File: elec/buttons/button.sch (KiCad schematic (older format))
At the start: 6 parts, among them SW1 SW_PUSH, U1 moteino

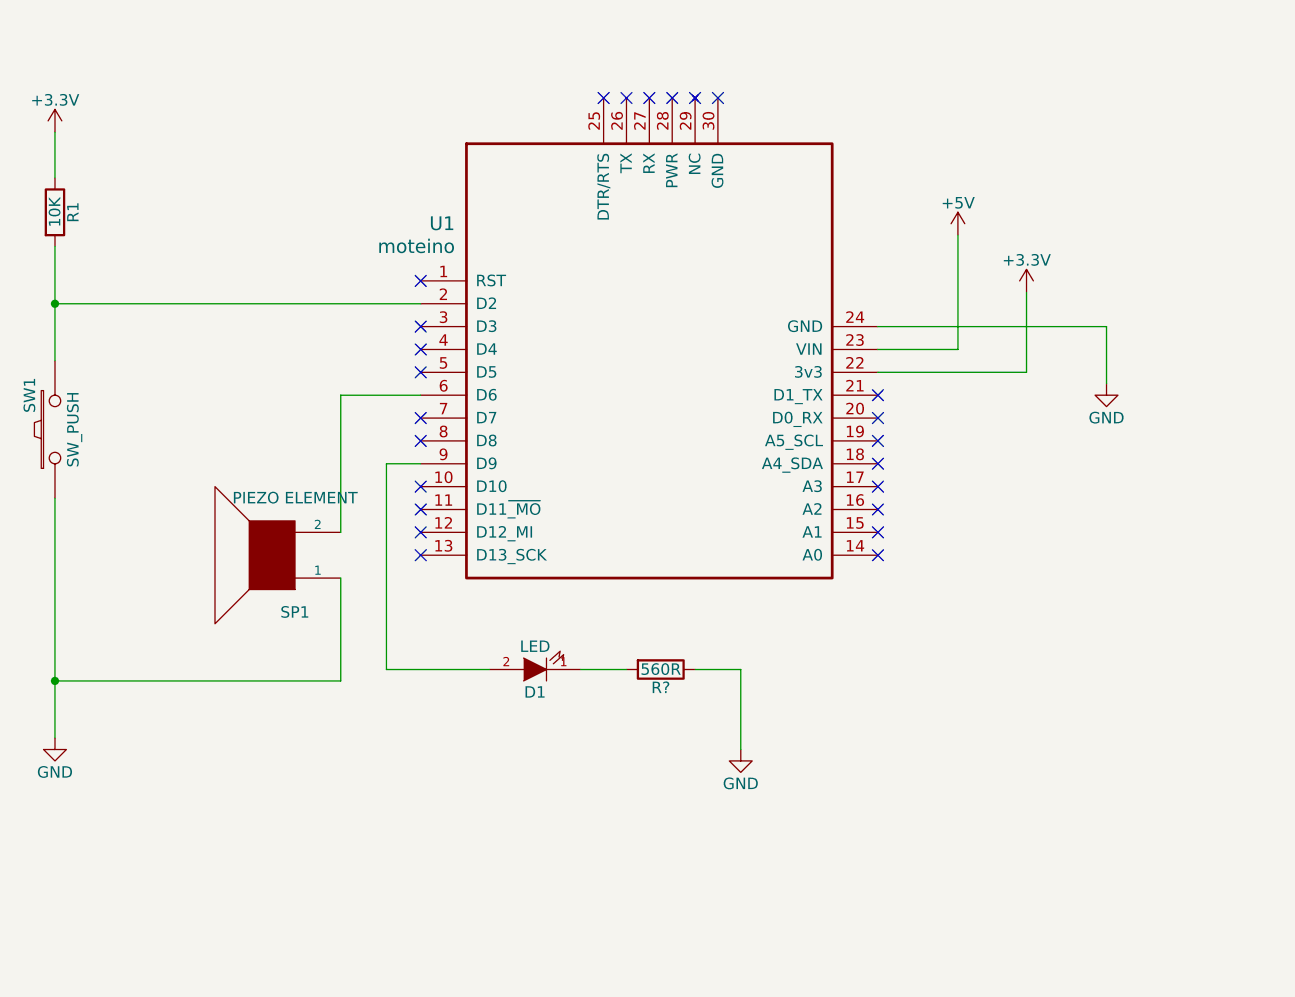
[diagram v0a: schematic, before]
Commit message: updated button schematic
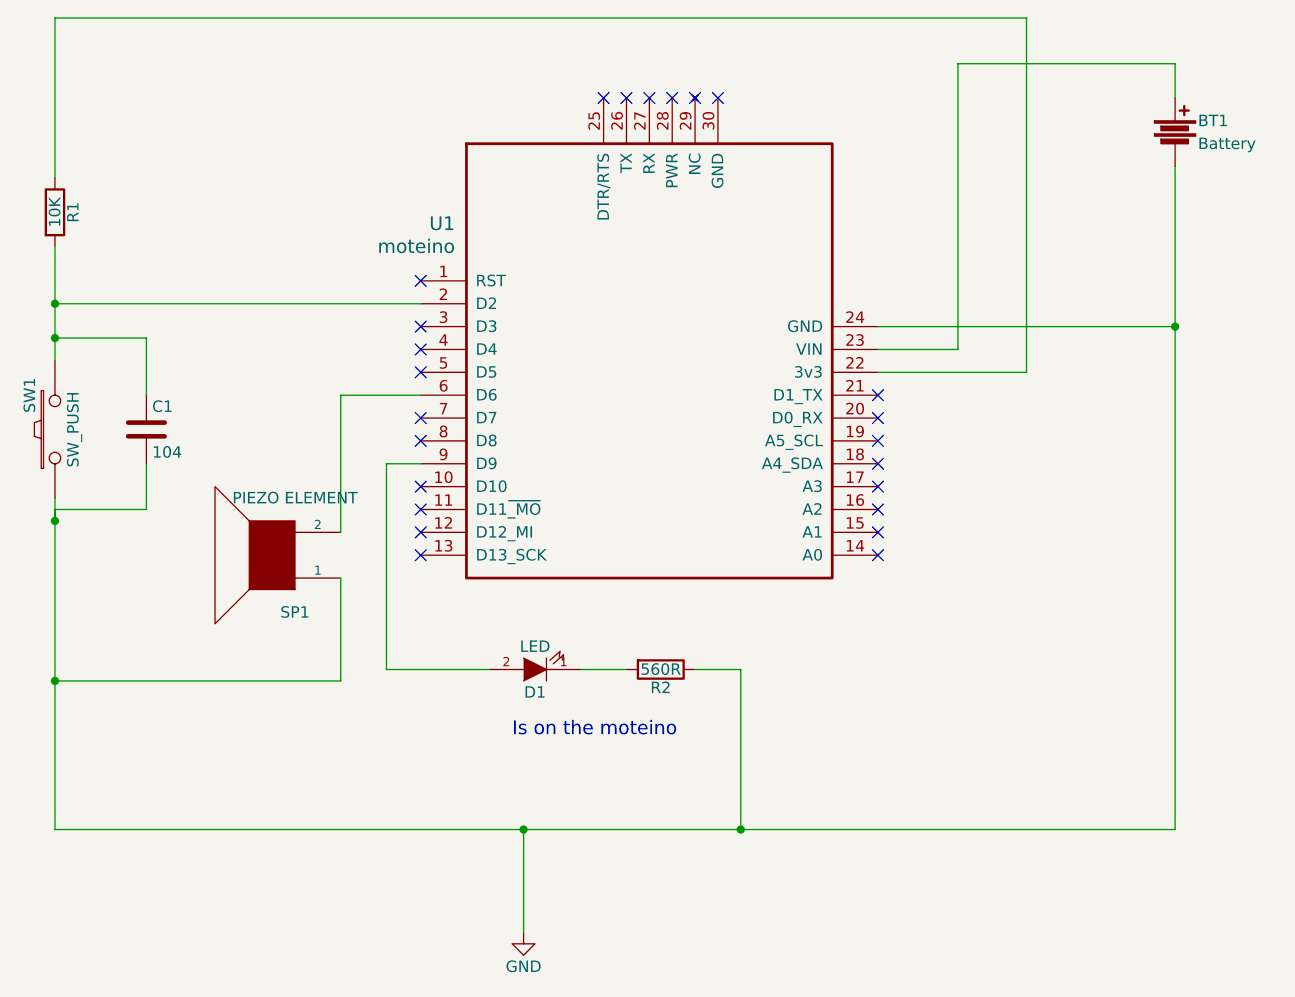
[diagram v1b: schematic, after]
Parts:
- added BT1: Battery, symbol Battery
- added C1: 104, symbol C
- gave numbers to parts that had none: 1
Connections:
- net GND: now also BT1.2, C1.2
- net at R1.2, SW1.2, U1.2 (D2): now also C1.1
- net +3V3: no longer names the net of R1.1, U1.22 (3v3)
- net +5V: no longer names the net of U1.23 (VIN)
- net +5V: now also BT1.1
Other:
- note added: "Is on the moteino"
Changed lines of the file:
@@
 $EndDescr
-$Comp
-L GND #PWR2
-U 1 1 57DAD49F
-P 2500 4650
-F 0 "#PWR2" H 2500 4400 50  0001 C CNN
-F 1 "GND" H 2500 4500 50  0000 C CNN
-F 2 "" H 2500 4650 50  0000 C CNN
-F 3 "" H 2500 4650 50  0000 C CNN
-	1    2500 4650
-	1    0    0    -1
-$EndComp
 $Comp
 L moteino U1
@@
 	2500 2500 2500 3000
 Wire Wire Line
-	2500 3600 2500 4650
+	2500 3600 2500 5050
 Wire Wire Line
 	4100 3150 3750 3150
@@
 Wire Wire Line
 	3950 4350 4400 4350
-$Comp
-L GND #PWR3
-U 1 1 57DADC66
-P 5500 4700
-F 0 "#PWR3" H 5500 4450 50  0001 C CNN
-F 1 "GND" H 5500 4550 50  0000 C CNN
-F 2 "" H 5500 4700 50  0000 C CNN
-F 3 "" H 5500 4700 50  0000 C CNN
-	1    5500 4700
-	1    0    0    -1
-$EndComp
 Wire Wire Line
 	4800 4350 5000 4350
-$Comp
-L +5V #PWR4
-U 1 1 57DADCB3
-P 6450 2450
-F 0 "#PWR4" H 6450 2300 50  0001 C CNN
-F 1 "+5V" H 6450 2590 50  0000 C CNN
-F 2 "" H 6450 2450 50  0000 C CNN
-F 3 "" H 6450 2450 50  0000 C CNN
-	1    6450 2450
-	1    0    0    -1
-$EndComp
-Wire Wire Line
-	6100 2950 6450 2950
-Wire Wire Line
-	6450 2950 6450 2450
-$Comp
-L GND #PWR6
-U 1 1 57DADCFF
-P 7100 3100
-F 0 "#PWR6" H 7100 2850 50  0001 C CNN
-F 1 "GND" H 7100 2950 50  0000 C CNN
-F 2 "" H 7100 3100 50  0000 C CNN
-F 3 "" H 7100 3100 50  0000 C CNN
-	1    7100 3100
-	1    0    0    -1
-$EndComp
-Wire Wire Line
-	6100 2850 7100 2850
-Wire Wire Line
-	7100 2850 7100 3100
-$Comp
-L +3.3V #PWR5
-U 1 1 57DADD30
-P 6750 2700
-F 0 "#PWR5" H 6750 2550 50  0001 C CNN
-F 1 "+3.3V" H 6750 2840 50  0000 C CNN
-F 2 "" H 6750 2700 50  0000 C CNN
-F 3 "" H 6750 2700 50  0000 C CNN
-	1    6750 2700
-	1    0    0    -1
-$EndComp
-Wire Wire Line
-	6100 3050 6750 3050
-Wire Wire Line
-	6750 3050 6750 2700
+Wire Wire Line
+	6450 2950 6100 2950
+Wire Wire Line
+	6450 1700 6450 2950
+Wire Wire Line
+	6100 2850 7400 2850
+Wire Wire Line
+	6750 3050 6100 3050
+Wire Wire Line
+	6750 1500 6750 3050
 NoConn ~ 6100 3150
 NoConn ~ 6100 3250
@@
 	1    0    0    -1
 $EndComp
-$Comp
-L +3.3V #PWR1
-U 1 1 57DADE5A
-P 2500 2000
-F 0 "#PWR1" H 2500 1850 50  0001 C CNN
-F 1 "+3.3V" H 2500 2140 50  0000 C CNN
-F 2 "" H 2500 2000 50  0000 C CNN
-F 3 "" H 2500 2000 50  0000 C CNN
-	1    2500 2000
-	1    0    0    -1
-$EndComp
-Wire Wire Line
-	2500 2000 2500 2200
+Wire Wire Line
+	2500 1500 2500 2200
 Connection ~ 2500 2750
 $Comp
-L R R?
+L R R2
 U 1 1 57DADEFB
 P 5150 4350
-F 0 "R?" V 5230 4350 50  0000 C CNN
+F 0 "R2" V 5230 4350 50  0000 C CNN
 F 1 "560R" V 5150 4350 50  0000 C CNN
 F 2 "" V 5080 4350 50  0000 C CNN
@@
 	5300 4350 5500 4350
 Wire Wire Line
-	5500 4350 5500 4700
+	5500 4350 5500 5050
+$Comp
+L Battery BT1
+U 1 1 57E2A99B
+P 7400 2000
+F 0 "BT1" H 7500 2050 50  0000 L CNN
+F 1 "Battery" H 7500 1950 50  0000 L CNN
+F 2 "" V 7400 2040 50  0000 C CNN
+F 3 "" V 7400 2040 50  0000 C CNN
+	1    7400 2000
+	1    0    0    -1
+$EndComp
+Wire Wire Line
+	6450 1700 7400 1700
+Wire Wire Line
+	7400 1700 7400 1850
+Wire Wire Line
+	7400 2150 7400 5050
+Wire Wire Line
+	6750 1500 2500 1500
+Text Notes 4500 4650 0    60   ~ 0
+Is on the moteino
+Wire Wire Line
+	7400 5050 2500 5050
+Connection ~ 7400 2850
+Connection ~ 5500 5050
+$Comp
+L C C1
+U 1 1 57E2AB61
+P 2900 3300
+F 0 "C1" H 2925 3400 50  0000 L CNN
+F 1 "104" H 2925 3200 50  0000 L CNN
+F 2 "" H 2938 3150 50  0000 C CNN
+F 3 "" H 2900 3300 50  0000 C CNN
+F 4 "~" H 2900 3300 60  0001 C CNN "Characteristics"
+F 5 "~" H 2900 3300 60  0001 C CNN "Description"
+F 6 "~" H 2900 3300 60  0001 C CNN "Package ID"
+F 7 "~" H 2900 3300 60  0001 C CNN "Source"
+F 8 "~" H 2900 3300 60  0001 C CNN "Critical"
+F 9 "~" H 2900 3300 60  0001 C CNN "Notes"
+F 10 "~" H 2900 3300 60  0001 C CNN "MFP"
+F 11 "~" H 2900 3300 60  0001 C CNN "supplier1_name"
+F 12 "~" H 2900 3300 60  0001 C CNN "supplier2_name"
+F 13 "~" H 2900 3300 60  0001 C CNN "supplier1_link"
+F 14 "~" H 2900 3300 60  0001 C CNN "supplier2_link"
+F 15 "~" H 2900 3300 60  0001 C CNN "MFN"
+	1    2900 3300
+	1    0    0    -1
+$EndComp
+Wire Wire Line
+	2900 3150 2900 2900
+Wire Wire Line
+	2900 2900 2500 2900
+Connection ~ 2500 2900
+Wire Wire Line
+	2900 3450 2900 3650
+Wire Wire Line
+	2900 3650 2500 3650
+Wire Wire Line
+	2500 3650 2500 3700
+Connection ~ 2500 3700
+$Comp
+L GND #PWR?
+U 1 1 57E2AC3A
+P 4550 5500
+F 0 "#PWR?" H 4550 5250 50  0001 C CNN
+F 1 "GND" H 4550 5350 50  0000 C CNN
+F 2 "" H 4550 5500 50  0000 C CNN
+F 3 "" H 4550 5500 50  0000 C CNN
+	1    4550 5500
+	1    0    0    -1
+$EndComp
+Wire Wire Line
+	4550 5500 4550 5050
+Connection ~ 4550 5050
 $EndSCHEMATC
